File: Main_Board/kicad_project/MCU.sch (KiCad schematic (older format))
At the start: 33 parts, among them J13 DEBUG_HEADER, SW1 SW_SPST, U9 STM32G474VxT, Y1 ABS06-32.768kHz, Y2 DNP

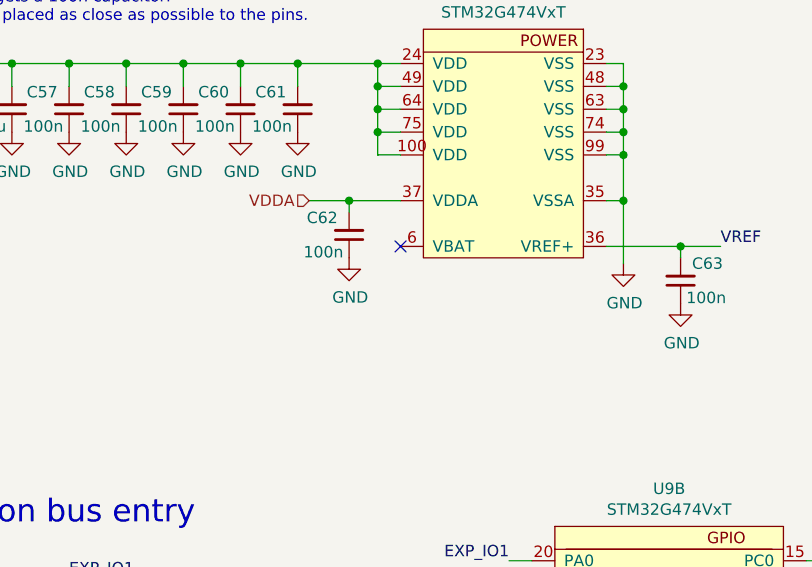
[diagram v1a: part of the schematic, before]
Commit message: Main board sch: add backup battery, update license
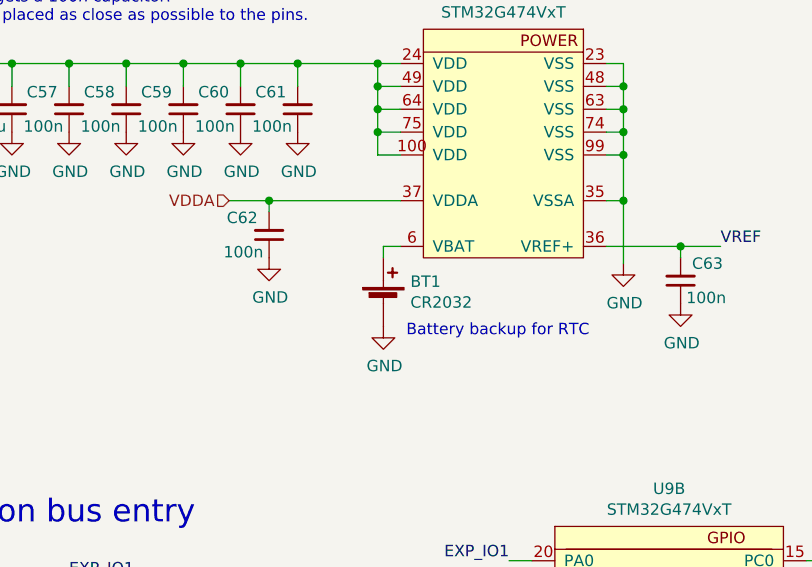
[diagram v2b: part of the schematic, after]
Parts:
- added BT1: CR2032, LoaDy:CR2032_SMD, symbol Device:Battery_Cell
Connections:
- net GND: now also BT1.2 (-)
- net at U9.6 (VBAT): now also BT1.1 (+)
- no-connect marks 1 -> 0
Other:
- note added: "Battery backup for RTC"
- moved on the sheet: C62
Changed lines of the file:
@@
 Sheet 8 10
 Title "Cube Main Board - MCU & Debug"
-Date "2020-09-23"
-Rev "1"
+Date "2020-10-02"
+Rev "1.1"
 Comp "Oldřich Pecák (LoaDy)"
-Comment1 "Licensed under CERN-OHL-P v2"
+Comment1 "Licensed under CERN-OHL-W v2"
 Comment2 ""
 Comment3 ""
@@
 L Device:C_Small C62
 U 1 1 5F509E58
-P 3050 2700
-F 0 "C62" H 3000 2625 50  0000 R CNN
-F 1 "100n" H 3025 2775 50  0000 R CNN
-F 2 "Capacitor_SMD:C_0603_1608Metric" H 3050 2700 50  0001 C CNN
-F 3 "~" H 3050 2700 50  0001 C CNN
-	1    3050 2700
+P 2700 2700
+F 0 "C62" H 2650 2625 50  0000 R CNN
+F 1 "100n" H 2675 2775 50  0000 R CNN
+F 2 "Capacitor_SMD:C_0603_1608Metric" H 2700 2700 50  0001 C CNN
+F 3 "~" H 2700 2700 50  0001 C CNN
+	1    2700 2700
 	1    0    0    1
 $EndComp
@@
 L power:GND #PWR068
 U 1 1 5F50A4F3
-P 3050 2800
-F 0 "#PWR068" H 3050 2550 50  0001 C CNN
-F 1 "GND" H 3055 2627 50  0000 C CNN
-F 2 "" H 3050 2800 50  0001 C CNN
-F 3 "" H 3050 2800 50  0001 C CNN
-	1    3050 2800
-	1    0    0    -1
-$EndComp
-Wire Wire Line
-	3275 2550 3050 2550
-Wire Wire Line
-	3050 2600 3050 2550
-Connection ~ 3050 2550
-Wire Wire Line
-	3050 2550 2875 2550
-Text HLabel 2875 2550 0    50   Input ~ 0
+P 2700 2800
+F 0 "#PWR068" H 2700 2550 50  0001 C CNN
+F 1 "GND" H 2705 2627 50  0000 C CNN
+F 2 "" H 2700 2800 50  0001 C CNN
+F 3 "" H 2700 2800 50  0001 C CNN
+	1    2700 2800
+	1    0    0    -1
+$EndComp
+Wire Wire Line
+	2700 2600 2700 2550
+Connection ~ 2700 2550
+Wire Wire Line
+	2700 2550 2525 2550
+Text HLabel 2525 2550 0    50   Input ~ 0
 VDDA
 $Comp
@@
 Text Label 3750 4925 2    50   ~ 0
 EXP_IO9
-NoConn ~ 3275 2750
 $Comp
 L Device:Crystal_GND24_Small Y2
@@
 Text Notes 6000 2600 0    100  ~ 0
 Debug header
+$Comp
+L Device:Battery_Cell BT1
+U 1 1 5F78FF28
+P 3200 3000
+F 0 "BT1" H 3318 3096 50  0000 L CNN
+F 1 "CR2032" H 3318 3005 50  0000 L CNN
+F 2 "LoaDy:CR2032_SMD" H 3318 2959 50  0001 L CNN
+F 3 "~" V 3200 3060 50  0001 C CNN
+	1    3200 3000
+	1    0    0    -1
+$EndComp
+Wire Wire Line
+	2700 2550 3275 2550
+Wire Wire Line
+	3275 2750 3200 2750
+$Comp
+L power:GND #PWR0121
+U 1 1 5F7DE995
+P 3200 3100
+F 0 "#PWR0121" H 3200 2850 50  0001 C CNN
+F 1 "GND" H 3205 2927 50  0000 C CNN
+F 2 "" H 3200 3100 50  0001 C CNN
+F 3 "" H 3200 3100 50  0001 C CNN
+	1    3200 3100
+	1    0    0    -1
+$EndComp
+Wire Wire Line
+	3200 2800 3200 2750
+Text Notes 3300 3150 0    50   ~ 0
+Battery backup for RTC
 Wire Bus Line
 	8125 5225 8125 6200
